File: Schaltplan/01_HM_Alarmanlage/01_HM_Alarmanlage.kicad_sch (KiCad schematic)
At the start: 38 parts, among them J1 Ultraschallsensor, J2 I2C Display, J3 Header-7x2, J4 Conn_01x04, J5 IRL_Sensor, J6 Powerbank, J7 Conn_01x04, J8 Conn_01x03, J9 Conn_01x02, Q1 IRLB8721PBF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

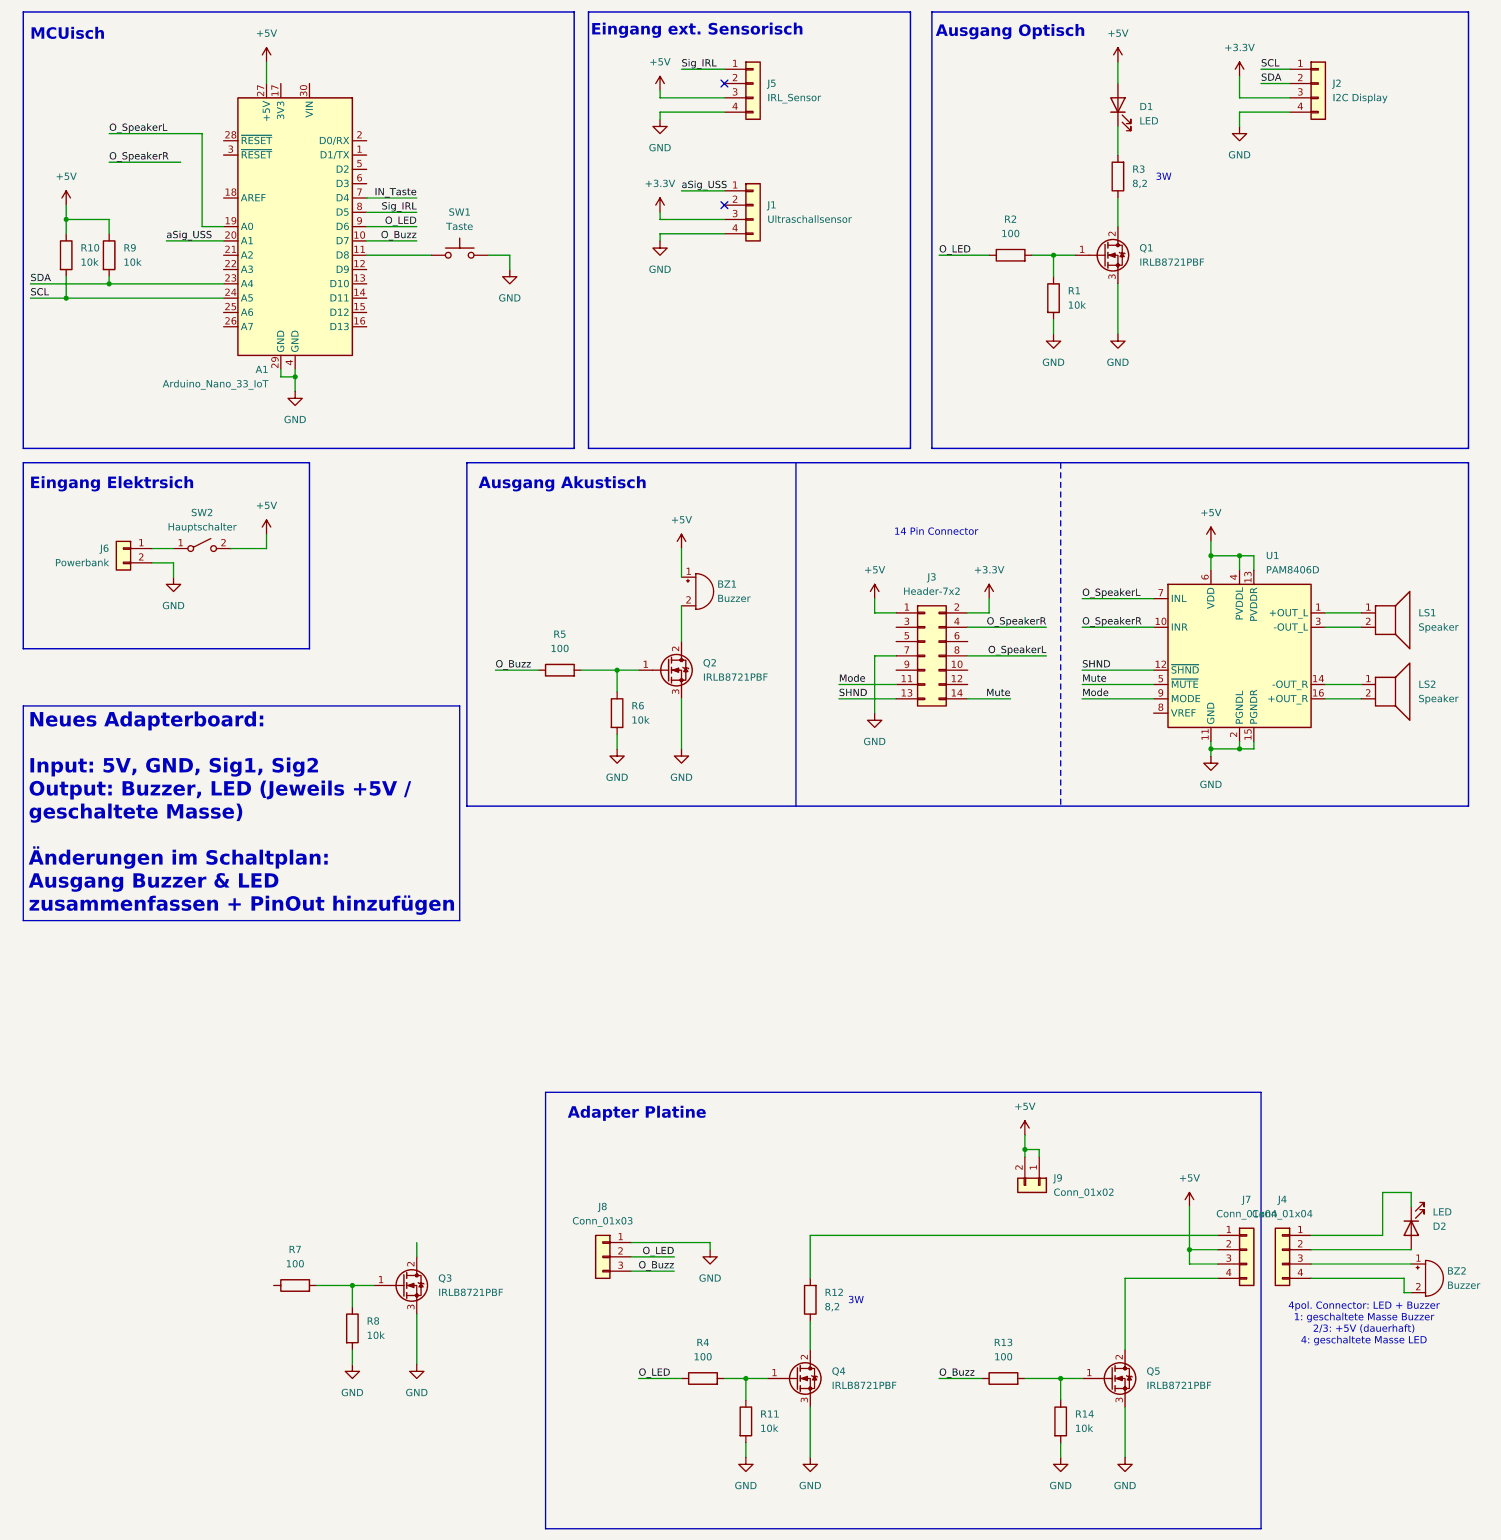
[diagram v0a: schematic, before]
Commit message: change: PinOuts korrigiert / angepasst. add: Bilder von PinOuts für AdapterPCB und Lautsprecher modul
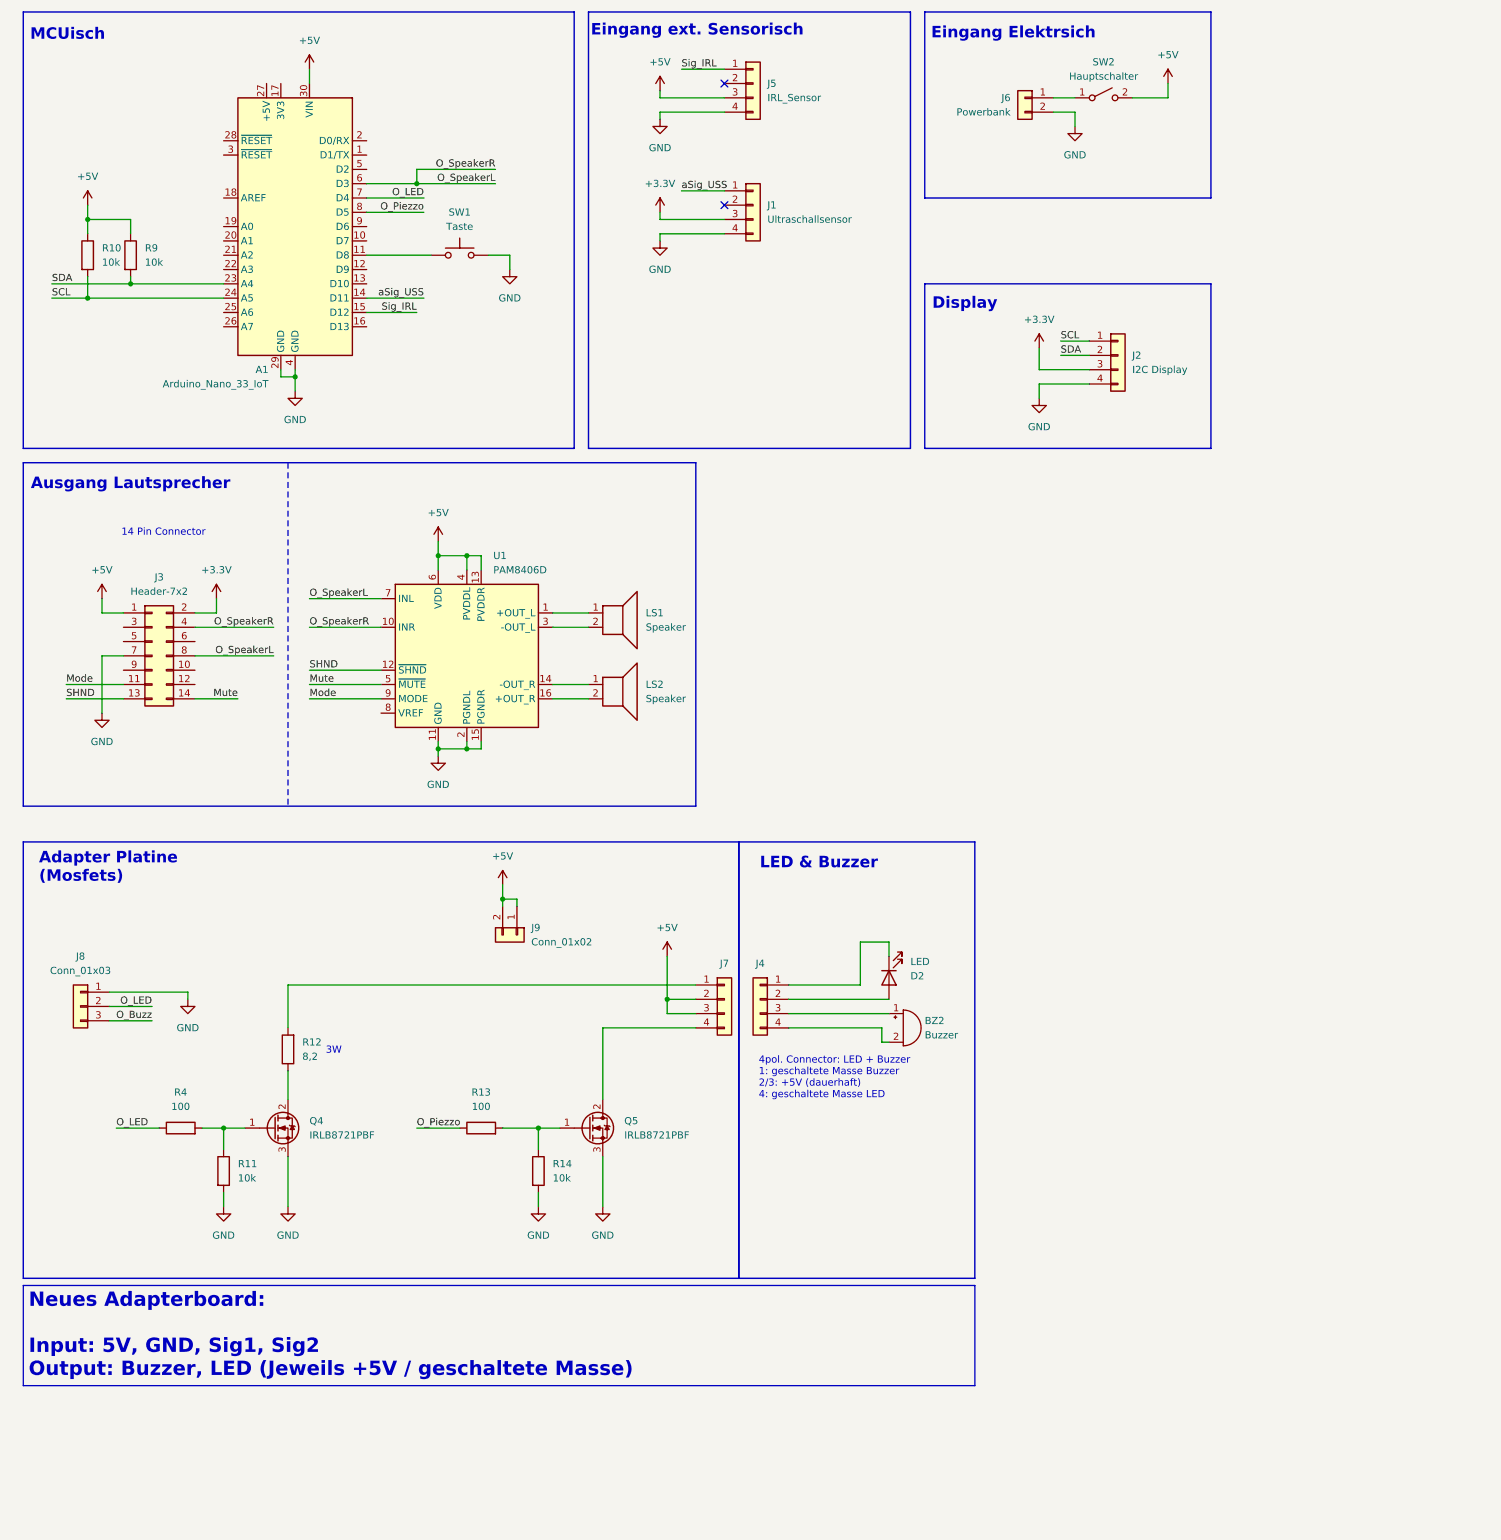
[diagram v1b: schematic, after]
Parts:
- removed BZ1: Buzzer, symbol Device:Buzzer
- removed D1: LED, symbol Device:LED
- removed Q1, Q2, Q3: IRLB8721PBF, Package_TO_SOT_THT:TO-220-3_Vertical, symbol Transistor_FET:IRLB8721PBF
- removed R1, R6, R8: 10k, symbol Device:R
- removed R2, R5, R7: 100, symbol Device:R
- removed R3: 8,2, symbol Device:R
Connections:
- net IN_Taste is gone; now on net O_LED: A1.7 (D4)
- net O_SpeakerR is gone; now on net O_SpeakerL: J3.4 (Pin_4), U1.10 (INR)
- net +5V: now also A1.30 (VIN); no longer A1.27 (+5V)
- net O_Buzz: no longer A1.10 (D7), R13.1
- net O_LED: no longer A1.9 (D6)
- net O_SpeakerL: now also A1.6 (D3); no longer A1.19 (A0)
- net Sig_IRL: now also A1.15 (D12); no longer A1.8 (D5)
- net aSig_USS: now also A1.14 (D11); no longer A1.20 (A1)
- new net O_Piezzo: A1.8 (D5), R13.1
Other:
- note added: "Adapter Platine (Mosfets)"
- note added: "Ausgang Lautsprecher"
- note added: "Display"
- note added: "LED & Buzzer"
- note removed: "Adapter Platine"
- note removed: "Ausgang Akustisch"
- note removed: "Ausgang Optisch"
- moved on the sheet: BZ2, D2, J2, J3, J4, J6, J7, J8, J9, LS1, LS2, Q4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

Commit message: change: Schaltplan auf 3x Buzzer angepasst & Lautsprecher als "Nicht verwendet" auf zweite Schaltplanseite ausgelagert
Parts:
- removed J3: Header-7x2, symbol Connector_Generic:Conn_02x07_Odd_Even
- removed LS1, LS2: Speaker, symbol Device:Speaker
- removed U1: PAM8406D, Package_SO:SOIC-16_3.9x9.9mm_P1.27mm, symbol Amplifier_Audio:PAM8406D
- added BZ1, BZ3: Buzzer, symbol Device:Buzzer
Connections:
- net at BZ2.1 (+), J4.3 (Pin_3): now also BZ1.1 (+), BZ3.1 (+)
- net at BZ2.2 (-), J4.4 (Pin_4): now also BZ1.2 (-), BZ3.2 (-)
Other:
- added sheet Lautsprecher (Lautsprecher.kicad_sch)
- note added: "Eingang"
- note added: "Eingang ext. Sensorik"
- note added: "MCU"
- note added: "NICHT Verwendet!"
- note removed: "14 Pin Connector"
- note removed: "Ausgang Lautsprecher"
- note removed: "Eingang Elektrsich"
- note removed: "Eingang ext. Sensorisch"
- note removed: "MCUisch"
- moved on the sheet: BZ2, D2, J4, J7, J8, J9, Q4, Q5, R11, R12, R13, R14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

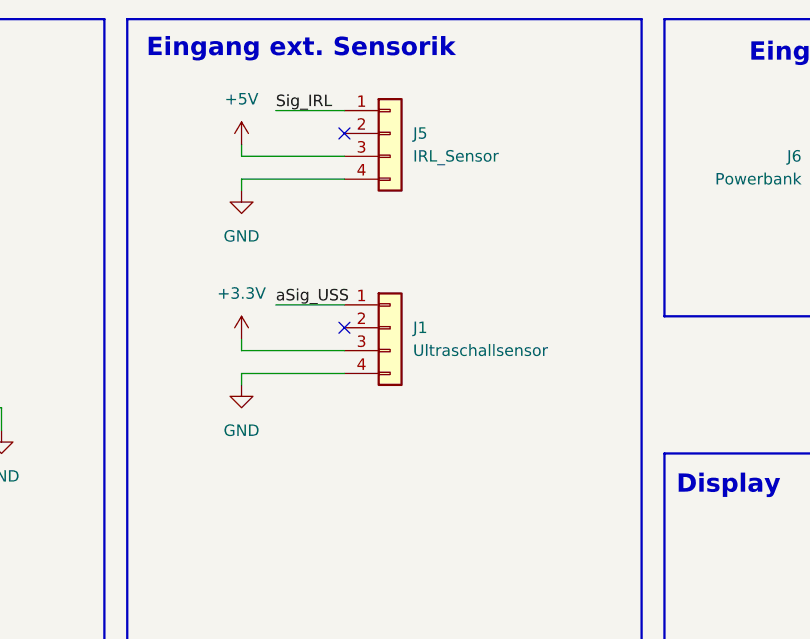
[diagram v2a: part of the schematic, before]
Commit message: fix: Schaltplan PinOut IRL-Sensor
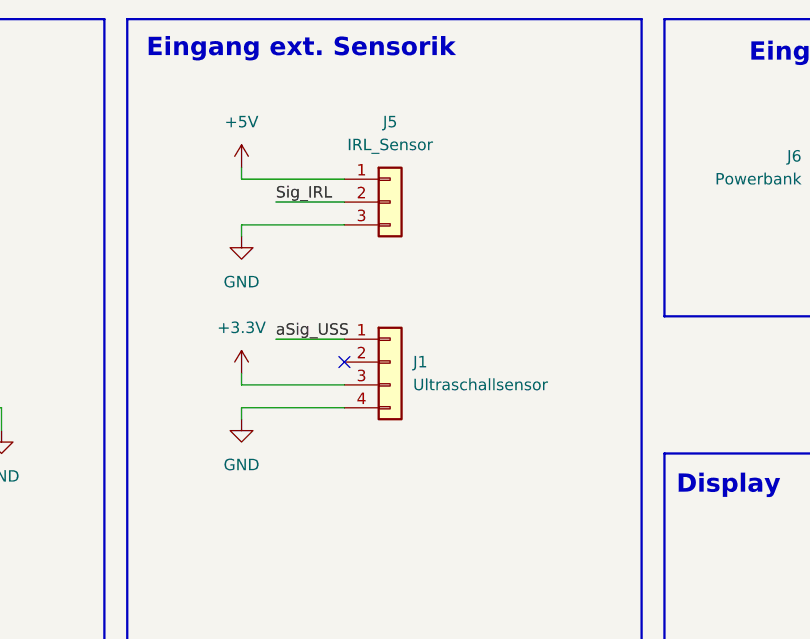
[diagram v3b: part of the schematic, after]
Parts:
- removed J5: IRL_Sensor, symbol Connector_Generic:Conn_01x04
- added J5: IRL_Sensor, symbol Connector_Generic:Conn_01x03
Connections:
- net +5V: now also J5.1 (Pin_1)
- net GND: now also J5.3 (Pin_3)
- net Sig_IRL: now also J5.2 (Pin_2)
- no-connect marks 2 -> 1
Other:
- moved on the sheet: J1
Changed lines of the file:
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@@
 	)
 	(no_connect
-		(at 144.78 54.61)
-	)
-	(no_connect
-		(at 144.78 33.02)
+		(at 144.78 58.42)
 	)
 	(wire
@@
 	(wire
 		(pts
-			(xy 137.16 52.07) (xy 144.78 52.07)
+			(xy 137.16 55.88) (xy 144.78 55.88)
 		)
 		(stroke
@@
 	(wire
 		(pts
-			(xy 133.35 38.1) (xy 144.78 38.1)
+			(xy 133.35 43.18) (xy 144.78 43.18)
 		)
 		(stroke
@@
 	(wire
 		(pts
-			(xy 133.35 35.56) (xy 144.78 35.56)
+			(xy 133.35 38.1) (xy 144.78 38.1)
 		)
 		(stroke
@@
 	(wire
 		(pts
-			(xy 133.35 57.15) (xy 144.78 57.15)
+			(xy 133.35 60.96) (xy 144.78 60.96)
 		)
 		(stroke
@@
 	(wire
 		(pts
-			(xy 133.35 60.96) (xy 133.35 59.69)
+			(xy 133.35 64.77) (xy 133.35 63.5)
 		)
 		(stroke
@@
 	(wire
 		(pts
-			(xy 133.35 59.69) (xy 144.78 59.69)
+			(xy 133.35 63.5) (xy 144.78 63.5)
 		)
 		(stroke
@@
 	(wire
 		(pts
-			(xy 133.35 34.29) (xy 133.35 35.56)
+			(xy 133.35 36.83) (xy 133.35 38.1)
 		)
 		(stroke
@@
 	(wire
 		(pts
-			(xy 137.16 30.48) (xy 144.78 30.48)
+			(xy 137.16 40.64) (xy 144.78 40.64)
 		)
 		(stroke
@@
 	(wire
 		(pts
-			(xy 133.35 55.88) (xy 133.35 57.15)
+			(xy 133.35 59.69) (xy 133.35 60.96)
 		)
 		(stroke
@@
 	(wire
 		(pts
-			(xy 133.35 39.37) (xy 133.35 38.1)
+			(xy 133.35 44.45) (xy 133.35 43.18)
 		)
 		(stroke
@@
 	)
 	(label "Sig_IRL"
-		(at 137.16 30.48 0)
+		(at 137.16 40.64 0)
 		(effects
 			(font
@@
 	)
 	(label "aSig_USS"
-		(at 137.16 52.07 0)
+		(at 137.16 55.88 0)
 		(effects
 			(font
@@
 	)
 	(symbol
-		(lib_id "Connector_Generic:Conn_01x04")
-		(at 149.86 33.02 0)
-		(unit 1)
-		(exclude_from_sim no)
-		(in_bom yes)
-		(on_board yes)
-		(dnp no)
-		(fields_autoplaced yes)
-		(property "Reference" "J5"
-			(at 152.4 33.0199 0)
-			(effects
-				(font
-					(size 1.27 1.27)
-				)
-				(justify left)
-			)
-		)
-		(property "Value" "IRL_Sensor"
-			(at 152.4 35.5599 0)
-			(effects
-				(font
-					(size 1.27 1.27)
-				)
-				(justify left)
-			)
-		)
-		(property "Footprint" ""
-			(at 149.86 33.02 0)
-			(effects
-				(font
-					(size 1.27 1.27)
-				)
-				(hide yes)
-			)
-		)
-		(property "Datasheet" "~"
-			(at 149.86 33.02 0)
-			(effects
-				(font
-					(size 1.27 1.27)
-				)
-				(hide yes)
-			)
-		)
-		(property "Description" "Generic connector, single row, 01x04, script generated (kicad-library-utils/schlib/autogen/connector/)"
-			(at 149.86 33.02 0)
-			(effects
-				(font
-					(size 1.27 1.27)
-				)
-				(hide yes)
-			)
-		)
-		(pin "1"
-		)
-		(pin "3"
-		)
-		(pin "4"
-		)
-		(pin "2"
-		)
-		(instances
-			(project "01_HM_Alarmanlage"
-				(path "/b8bd7eb2-83bb-4083-beb0-f753ccb9990f"
-					(reference "J5")
-					(unit 1)
-				)
-			)
-		)
-	)
-	(symbol
 		(lib_id "power:GND")
 		(at 106.68 66.04 0)
@@
 	(symbol
 		(lib_id "Connector_Generic:Conn_01x04")
-		(at 149.86 54.61 0)
+		(at 149.86 58.42 0)
 		(unit 1)
 		(exclude_from_sim no)
@@
 		(fields_autoplaced yes)
 		(property "Reference" "J1"
-			(at 152.4 54.6099 0)
+			(at 152.4 58.4199 0)
 			(effects
 				(font
@@
 		)
 		(property "Value" "Ultraschallsensor"
-			(at 152.4 57.1499 0)
+			(at 152.4 60.9599 0)
 			(effects
 				(font
@@
 		)
 		(property "Footprint" ""
-			(at 149.86 54.61 0)
+			(at 149.86 58.42 0)
 			(effects
 				(font
@@
 		)
 		(property "Datasheet" "~"
-			(at 149.86 54.61 0)
+			(at 149.86 58.42 0)
 			(effects
 				(font
@@
 		)
 		(property "Description" "Generic connector, single row, 01x04, script generated (kicad-library-utils/schlib/autogen/connector/)"
-			(at 149.86 54.61 0)
+			(at 149.86 58.42 0)
 			(effects
 				(font
@@
 	(symbol
 		(lib_id "power:GND")
-		(at 133.35 39.37 0)
+		(at 133.35 44.45 0)
 		(unit 1)
 		(exclude_from_sim no)
@@
 		(fields_autoplaced yes)
 		(property "Reference" "#PWR07"
-			(at 133.35 45.72 0)
+			(at 133.35 50.8 0)
 			(effects
 				(font
@@
 		)
 		(property "Value" "GND"
-			(at 133.35 44.45 0)
+			(at 133.35 49.53 0)
 			(effects
 				(font
@@
 		)
 		(property "Footprint" ""
-			(at 133.35 39.37 0)
+			(at 133.35 44.45 0)
 			(effects
 				(font
@@
 		)
 		(property "Datasheet" ""
-			(at 133.35 39.37 0)
+			(at 133.35 44.45 0)
 			(effects
 				(font
@@
 		)
 		(property "Description" "Power symbol creates a global label with name \"GND\" , ground"
-			(at 133.35 39.37 0)
+			(at 133.35 44.45 0)
 			(effects
 				(font
@@
 	(symbol
 		(lib_id "power:GND")
-		(at 133.35 60.96 0)
+		(at 133.35 64.77 0)
 		(unit 1)
 		(exclude_from_sim no)
@@
 		(fields_autoplaced yes)
 		(property "Reference" "#PWR010"
-			(at 133.35 67.31 0)
+			(at 133.35 71.12 0)
 			(effects
 				(font
@@
 		)
 		(property "Value" "GND"
-			(at 133.35 66.04 0)
+			(at 133.35 69.85 0)
 			(effects
 				(font
@@
 		)
 		(property "Footprint" ""
-			(at 133.35 60.96 0)
+			(at 133.35 64.77 0)
 			(effects
 				(font
@@
 		)
 		(property "Datasheet" ""
-			(at 133.35 60.96 0)
+			(at 133.35 64.77 0)
 			(effects
 				(font
@@
 		)
 		(property "Description" "Power symbol creates a global label with name \"GND\" , ground"
-			(at 133.35 60.96 0)
+			(at 133.35 64.77 0)
 			(effects
 				(font
@@
 	(symbol
 		(lib_id "power:+3.3V")
-		(at 133.35 55.88 0)
+		(at 133.35 59.69 0)
 		(unit 1)
 		(exclude_from_sim no)
@@
 		(fields_autoplaced yes)
 		(property "Reference" "#PWR09"
-			(at 133.35 59.69 0)
+			(at 133.35 63.5 0)
 			(effects
 				(font
@@
 		)
 		(property "Value" "+3.3V"
-			(at 133.35 50.8 0)
+			(at 133.35 54.61 0)
 			(effects
 				(font
@@
 		)
 		(property "Footprint" ""
-			(at 133.35 55.88 0)
+			(at 133.35 59.69 0)
 			(effects
 				(font
@@
 		)
 		(property "Datasheet" ""
-			(at 133.35 55.88 0)
+			(at 133.35 59.69 0)
 			(effects
 				(font
@@
 		)
 		(property "Description" "Power symbol creates a global label with name \"+3.3V\""
-			(at 133.35 55.88 0)
+			(at 133.35 59.69 0)
 			(effects
 				(font
@@
 	)
 	(symbol
+		(lib_id "Connector_Generic:Conn_01x03")
+		(at 149.86 40.64 0)
+		(unit 1)
+		(exclude_from_sim no)
+		(in_bom yes)
+		(on_board yes)
+		(dnp no)
+		(property "Reference" "J5"
+			(at 149.86 31.75 0)
+			(effects
+				(font
+					(size 1.27 1.27)
+				)
+			)
+		)
+		(property "Value" "IRL_Sensor"
+			(at 149.86 34.29 0)
+			(effects
+				(font
+					(size 1.27 1.27)
+				)
+			)
+		)
+		(property "Footprint" ""
+			(at 149.86 40.64 0)
+			(effects
+				(font
+					(size 1.27 1.27)
+				)
+				(hide yes)
+			)
+		)
+		(property "Datasheet" "~"
+			(at 149.86 40.64 0)
+			(effects
+				(font
+					(size 1.27 1.27)
+				)
+				(hide yes)
+			)
+		)
+		(property "Description" "Generic connector, single row, 01x03, script generated (kicad-library-utils/schlib/autogen/connector/)"
+			(at 149.86 40.64 0)
+			(effects
+				(font
+					(size 1.27 1.27)
+				)
+				(hide yes)
+			)
+		)
+		(pin "3"
+		)
+		(pin "2"
+		)
+		(pin "1"
+		)
+		(instances
+			(project "01_HM_Alarmanlage"
+				(path "/b8bd7eb2-83bb-4083-beb0-f753ccb9990f"
+					(reference "J5")
+					(unit 1)
+				)
+			)
+		)
+	)
+	(symbol
 		(lib_id "power:+5V")
-		(at 133.35 34.29 0)
+		(at 133.35 36.83 0)
 		(unit 1)
 		(exclude_from_sim no)
@@
 		(fields_autoplaced yes)
 		(property "Reference" "#PWR08"
-			(at 133.35 38.1 0)
+			(at 133.35 40.64 0)
 			(effects
 				(font
@@
 		)
 		(property "Value" "+5V"
-			(at 133.35 29.21 0)
+			(at 133.35 31.75 0)
 			(effects
 				(font
@@
 		)
 		(property "Footprint" ""
-			(at 133.35 34.29 0)
+			(at 133.35 36.83 0)
 			(effects
 				(font
@@
 		)
 		(property "Datasheet" ""
-			(at 133.35 34.29 0)
+			(at 133.35 36.83 0)
 			(effects
 				(font
@@
 		)
 		(property "Description" "Power symbol creates a global label with name \"+5V\""
-			(at 133.35 34.29 0)
+			(at 133.35 36.83 0)
 			(effects
 				(font
